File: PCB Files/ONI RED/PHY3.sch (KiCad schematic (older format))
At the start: 40 parts, among them J1 JK0654219, U4 KSZ9031RNXCA, Y1 25MHz

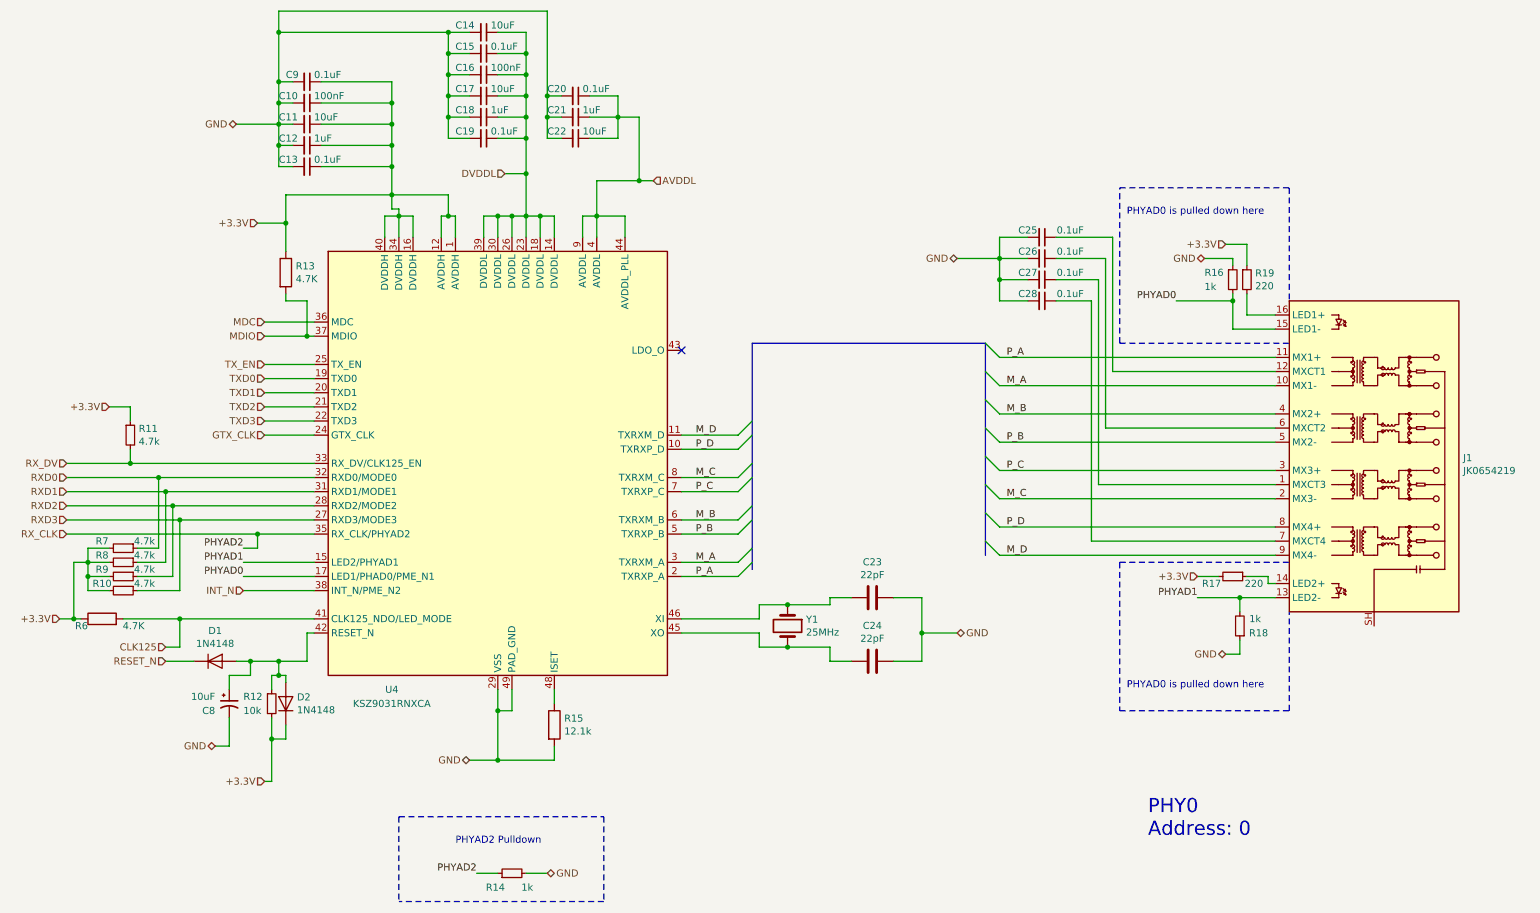
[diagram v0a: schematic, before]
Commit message: Added extra PHYs and expanded IO
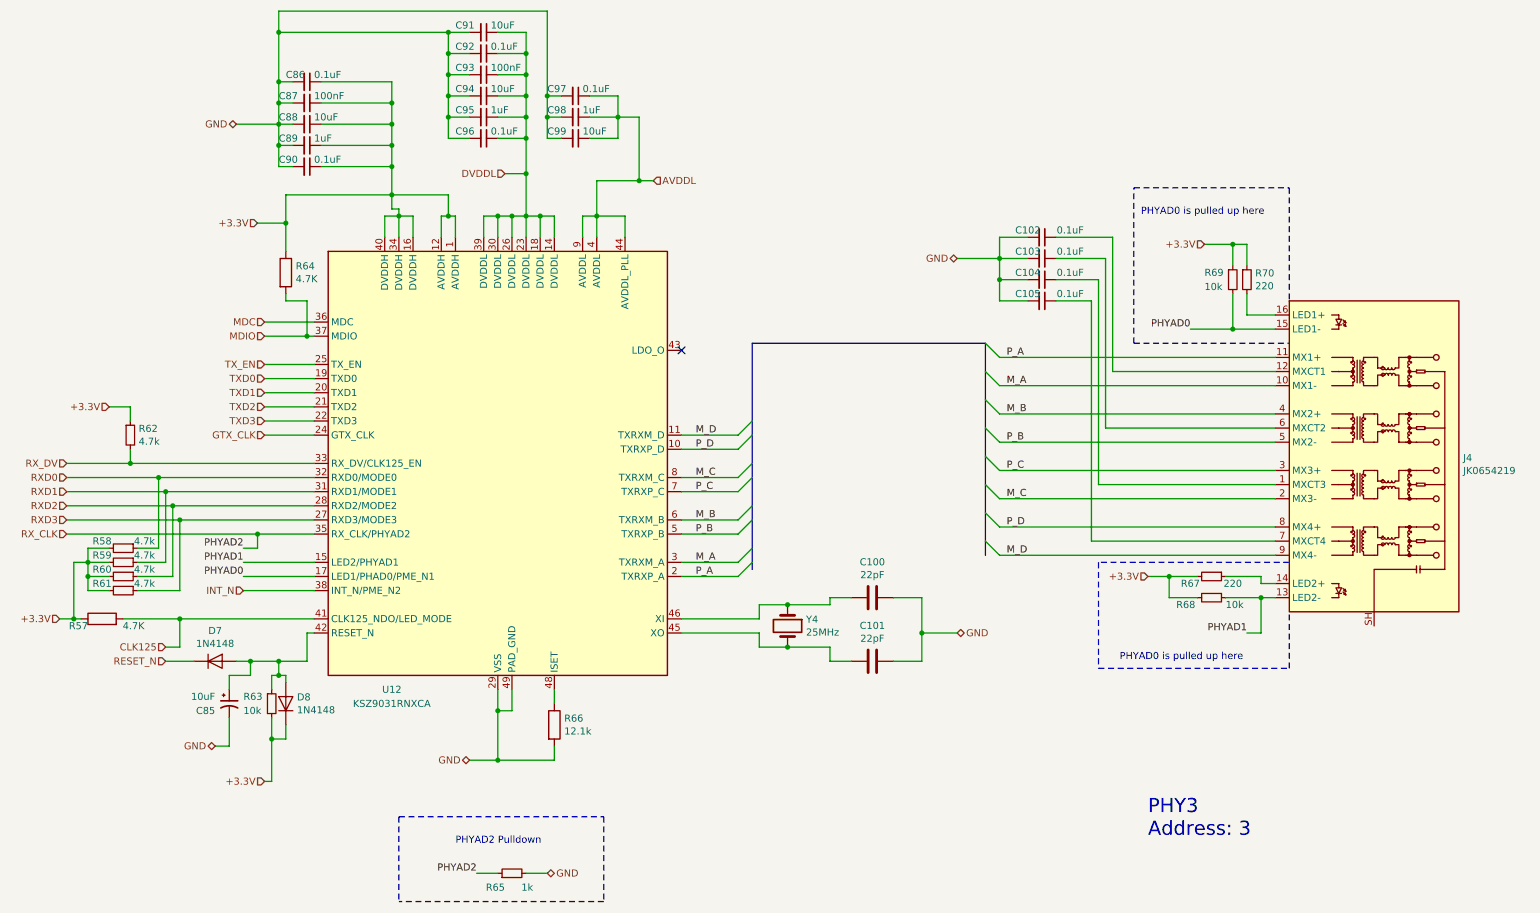
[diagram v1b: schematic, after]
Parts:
- removed C10, C16: 100nF, symbol Device:C_Small
- removed C11, C14, C17, C22: 10uF, symbol Device:C_Small
- removed C12, C18, C21: 1uF, symbol Device:C_Small
- removed C13, C15, C19, C20, C25, C26, C27, C28, C9: 0.1uF, symbol Device:C_Small
- removed C23, C24: 22pF, symbol Device:C
- removed C8: 10uF, symbol Device:CP1_Small
- removed D1, D2: 1N4148, symbol Device:D
- removed J1: JK0654219, Connector_RJ:RJ45_Pulse_JK0654219NL_Horizontal, symbol Connector:JK0654219
- removed R10, R11, R7, R8, R9: 4.7k, symbol Device:R_Small
- removed R12: 10k, symbol Device:R_Small
- removed R13, R6: 4.7K, symbol Device:R
- removed R14, R16, R18: 1k, symbol Device:R_Small
- removed R15: 12.1k, symbol Device:R
- removed R17, R19: 220, symbol Device:R_Small
- removed U4: KSZ9031RNXCA, Package_DFN_QFN:QFN-48-1EP_7x7mm_P0.5mm_EP5.15x5.15mm, symbol Interface_Ethernet:KSZ9031RNXCA
- removed Y1: 25MHz, symbol Device:Crystal
- added C100, C101: 22pF, symbol Device:C
- added C102, C103, C104, C105, C86, C90, C92, C96, C97: 0.1uF, symbol Device:C_Small
- added C85: 10uF, symbol Device:CP1_Small
- added C87, C93: 100nF, symbol Device:C_Small
- added C88, C91, C94, C99: 10uF, symbol Device:C_Small
- added C89, C95, C98: 1uF, symbol Device:C_Small
- added D7, D8: 1N4148, symbol Device:D
- added J4: JK0654219, Connector_RJ:RJ45_Pulse_JK0654219NL_Horizontal, symbol Connector:JK0654219
- added R57, R64: 4.7K, symbol Device:R
- added R58, R59, R60, R61, R62: 4.7k, symbol Device:R_Small
- added R63, R68, R69: 10k, symbol Device:R_Small
- added R65: 1k, symbol Device:R_Small
- added R66: 12.1k, symbol Device:R
- added R67, R70: 220, symbol Device:R_Small
- added U12: KSZ9031RNXCA, Package_DFN_QFN:QFN-48-1EP_7x7mm_P0.5mm_EP5.15x5.15mm, symbol Interface_Ethernet:KSZ9031RNXCA
- added Y4: 25MHz, symbol Device:Crystal
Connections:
- net +3.3V: now also C86.1, C87.1, C88.1, C89.1, C90.1, D8.1 (K), R57.1, R58.2, R59.2, R60.2, R61.2, R62.1, R63.2, R64.1, R67.2, R68.2, R69.1, R70.1, U12.1 (AVDDH), U12.12 (AVDDH), U12.16 (DVDDH), U12.34 (DVDDH), U12.40 (DVDDH)
- net AVDDL: now also C97.1, C98.1, C99.1, U12.4 (AVDDL), U12.44 (AVDDL_PLL), U12.9 (AVDDL)
- net CLK125: now also R57.2, U12.41 (CLK125_NDO/LED_MODE)
- net DVDDL: now also C91.1, C92.1, C93.1, C94.1, C95.1, C96.1, U12.14 (DVDDL), U12.18 (DVDDL), U12.23 (DVDDL), U12.26 (DVDDL), U12.30 (DVDDL), U12.39 (DVDDL)
- net GND: now also C100.1, C101.1, C102.2, C103.2, C104.2, C105.2, C85.2, C86.2, C87.2, C88.2, C89.2, C90.2, C91.2, C92.2, C93.2, C94.2, C95.2, C96.2, C97.2, C98.2, C99.2, R65.2, R66.2, U12.29 (VSS), U12.49 (PAD_GND)
- net GTX_CLK: now also U12.24 (GTX_CLK)
- net INT_N: now also U12.38 (INT_N/PME_N2)
- net MDC: now also U12.36 (MDC)
- net MDIO: now also R64.2, U12.37 (MDIO)
- net M_A: now also J4.10 (MX1-), U12.3 (TXRXM_A)
- net M_B: now also J4.4 (MX2+), U12.6 (TXRXM_B)
- net M_C: now also J4.2 (MX3-), U12.8 (TXRXM_C)
- net M_D: now also J4.9 (MX4-), U12.11 (TXRXM_D)
- net PHYAD0: now also J4.15 (LED1-), R69.2, U12.17 (LED1/PHAD0/PME_N1)
- net PHYAD1: now also J4.13 (LED2-), R68.1, U12.15 (LED2/PHYAD1)
- net P_A: now also J4.11 (MX1+), U12.2 (TXRXP_A)
- net P_B: now also J4.5 (MX2-), U12.5 (TXRXP_B)
- net P_C: now also J4.3 (MX3+), U12.7 (TXRXP_C)
- net P_D: now also J4.8 (MX4+), U12.10 (TXRXP_D)
- net RESET_N: now also D7.1 (K)
- net RXD0: now also R58.1, U12.32 (RXD0/MODE0)
- net RXD1: now also R59.1, U12.31 (RXD1/MODE1)
- net RXD2: now also R60.1, U12.28 (RXD2/MODE2)
- net RXD3: now also R61.1, U12.27 (RXD3/MODE3)
- net RX_CLK: now also R65.1, U12.35 (RX_CLK/PHYAD2)
- net RX_DV: now also R62.2, U12.33 (RX_DV/CLK125_EN)
- net TXD0: now also U12.19 (TXD0)
- net TXD1: now also U12.20 (TXD1)
- net TXD2: now also U12.21 (TXD2)
- net TXD3: now also U12.22 (TXD3)
- net TX_EN: now also U12.25 (TX_EN)
- new net: C85.1, D7.2 (A), D8.2 (A), R63.1, U12.42 (RESET_N)
- new net: C101.2, U12.45 (XO), Y4.2
- new net: C100.2, U12.46 (XI), Y4.1
- new net: R66.1, U12.48 (ISET)
- new net: C104.1, J4.1 (MXCT3)
- new net: C102.1, J4.12 (MXCT1)
- new net: J4.14 (LED2+), R67.1
- new net: J4.16 (LED1+), R70.2
- new net: C103.1, J4.6 (MXCT2)
- new net: C105.1, J4.7 (MXCT4)
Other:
- note added: "PHY3\nAddress: 3"
- note added: "PHYAD0 is pulled up here"
- note removed: "PHY0\nAddress: 0"
- note removed: "PHYAD0 is pulled down here"
